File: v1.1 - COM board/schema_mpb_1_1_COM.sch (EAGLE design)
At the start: 4 parts, among them IC1 E73_2G4M04S, U1 ESP-WROOM-32

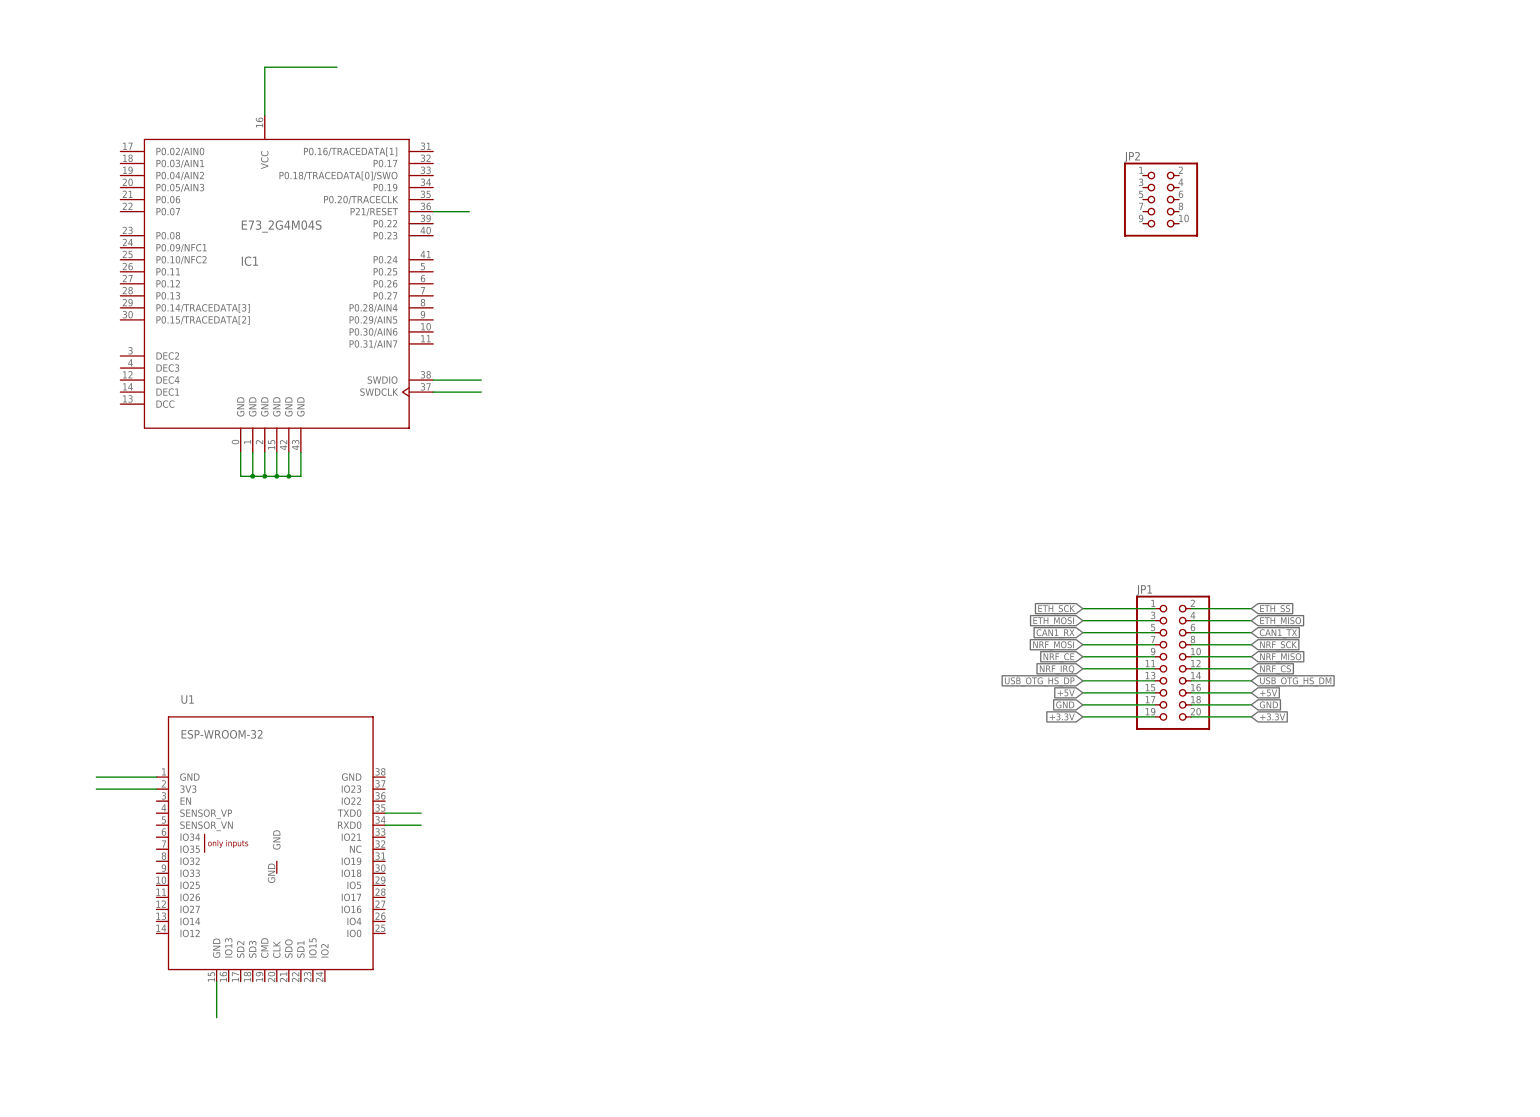
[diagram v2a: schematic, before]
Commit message: COM board
- Routed first version of Wireless COM board
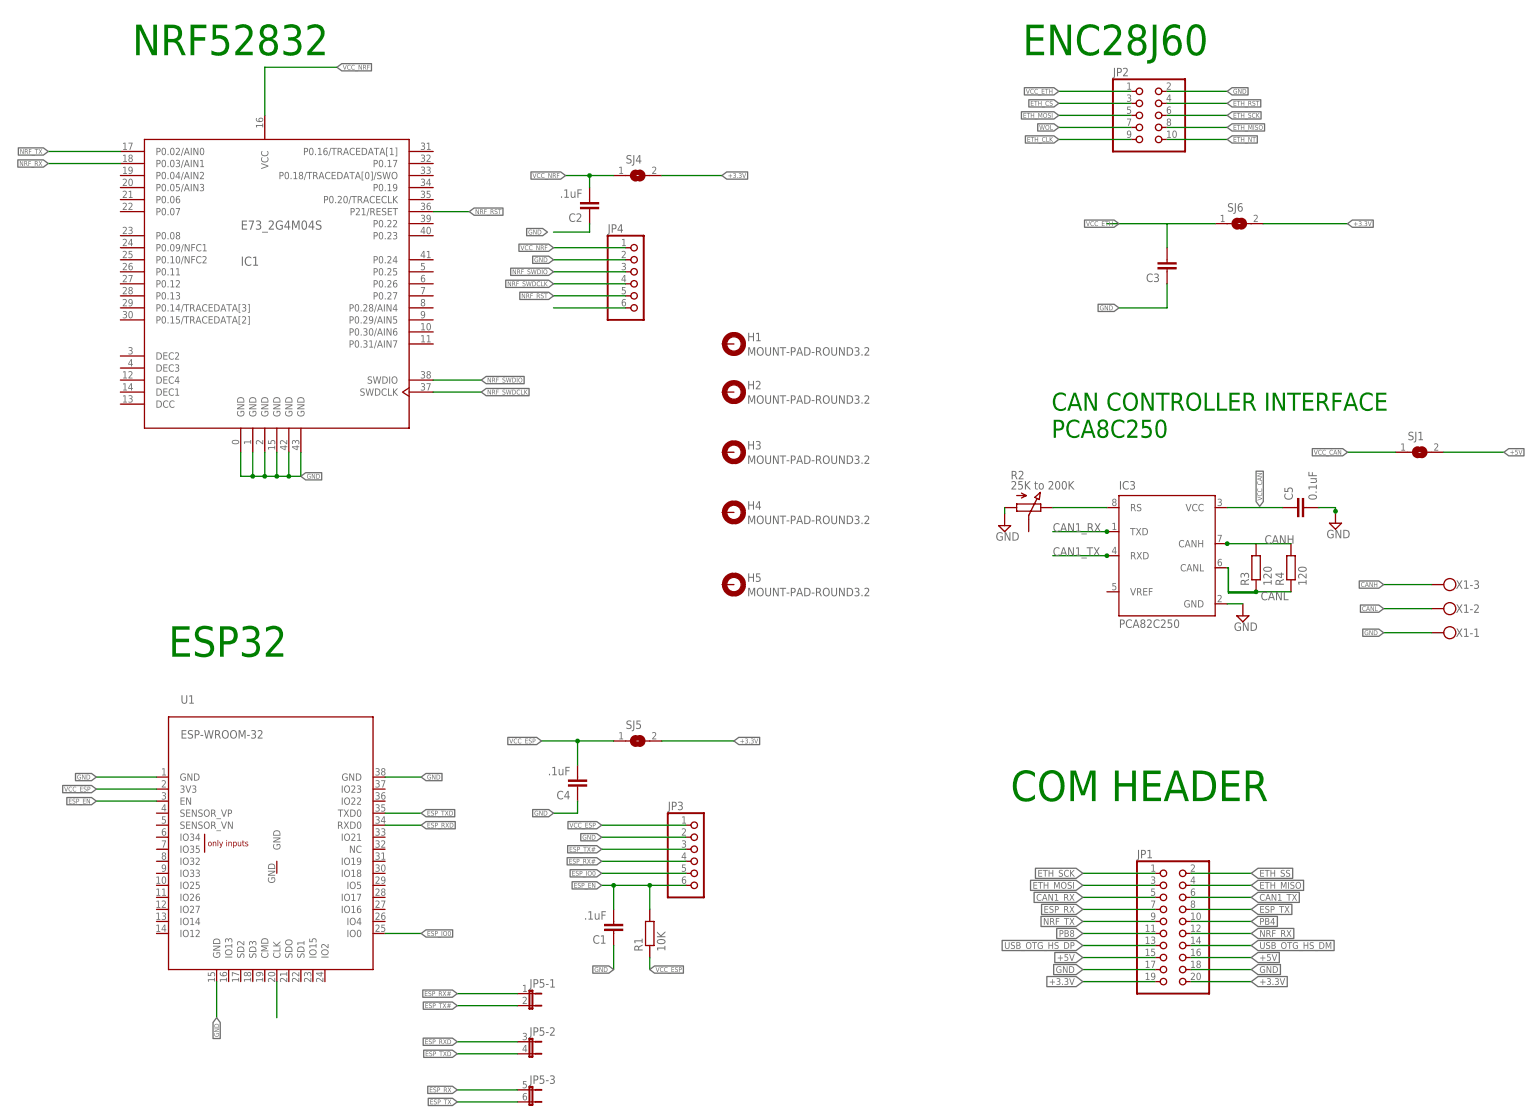
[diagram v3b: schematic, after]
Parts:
- added C1, C2, C4: .1uF, resistor:C-EUC0603
- added C3: (no value), resistor:C-EUC0603
- added C5: 0.1uF, resistor:C-EUC0805
- added H1, H2, H3, H4, H5: MOUNT-PAD-ROUND3.2, holes:MOUNT-PAD-ROUND3.2
- added IC3: PCA82C250, micro-philips:PCA82C250
- added JP3, JP4: (no value), pinhead:PINHD-1X6
- added JP5: (no value), jumper:JP3QE
- added R1: 10K, resistor:R-EU_R0603
- added R2: 25K to 200K, pot-vitrohm:PC25
- added R3, R4: 120, resistor:R-EU_R0805
- added SJ1, SJ4, SJ5, SJ6: (no value), jumper:SJW
- added X1: (no value), con-wago-500:W237-103
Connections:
- net NRF_IRQ renamed PB8
- net NRF_MISO renamed PB4
- removed net N$10: IC1.P21/RESET
- removed net N$2: U1.3V3
- removed net N$3: U1.TXD0
- removed net N$4: U1.RXD0
- removed net N$5: U1.GND@15
- removed net N$6: IC1.GND@1, IC1.GND@2, IC1.GND@3, IC1.GND@4, IC1.GND@5, IC1.GND@6
- removed net N$8: IC1.SWDCLK
- removed net N$9: IC1.VCC@1
- removed net NRF_CE: JP1.9
- removed net NRF_CS: JP1.12
- removed net NRF_MOSI: JP1.7
- removed net NRF_SCK: JP1.8
- new net CANH: IC3.CANH, R3.2, R4.2, X1-3.KL
- new net CANL: IC3.CANL, R3.1, R4.1, X1-2.KL
- new net ESP_EN: C1.2, JP3.6, R1.2, U1.EN
- new net ESP_IO0: JP3.5, U1.IO0
- new net ESP_RX: JP1.7, JP5-3.1
- new net ESP_RX#: JP3.4, JP5-1.1
- new net ESP_RXD: JP5-2.1, U1.RXD0
- new net ESP_TX: JP1.8, JP5-3.2
- new net ESP_TX#: JP3.3, JP5-1.2
- new net ESP_TXD: JP5-2.2, U1.TXD0
- new net ETH_CLK: JP2.9
- new net ETH_CS: JP2.3
- new net ETH_NT: JP2.10
- new net ETH_RST: JP2.4
- new net N$12: U1.CLK
- new net NRF_RST: IC1.P21/RESET, JP4.5
- new net NRF_RX: IC1.P0.03/AIN1, JP1.12
- new net NRF_SWDCLK: IC1.SWDCLK, JP4.4
- new net NRF_SWDIO: IC1.SWDIO, JP4.3
- new net NRF_TX: IC1.P0.02/AIN0, JP1.9
- new net VCC_CAN: C5.1, IC3.VCC, SJ1.1
- new net VCC_ESP: C4.2, JP3.1, R1.1, SJ5.1, U1.3V3
- new net VCC_ETH: C3.2, JP2.1, SJ6.1
- new net VCC_NRF: C2.2, IC1.VCC@1, JP4.1, SJ4.1
- new net WOL: JP2.7
- net +3.3V: now also SJ4.2, SJ5.2, SJ6.2
- net +5V: now also SJ1.2
- net CAN1_RX: now also IC3.TXD
- net CAN1_TX: now also IC3.RXD
- net ETH_MISO: now also JP2.8
- net ETH_MOSI: now also JP2.5
- net ETH_SCK: now also JP2.6
- net GND: now also C1.1, C2.1, C3.1, C4.1, C5.2, IC1.GND@1, IC1.GND@2, IC1.GND@3, IC1.GND@4, IC1.GND@5, IC1.GND@6, IC3.GND, JP2.2, JP3.2, JP4.2, R2.A, U1.GND@1, U1.GND@15, U1.GND@38, X1-1.KL
- net N$1: now also IC3.RS, R2.E; no longer U1.GND@1
- net N$7: now also JP4.6; no longer IC1.SWDIO
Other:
- note added: "CAN CONTROLLER INTERFACE PCA8C250"
- note added: "COM HEADER"
- note added: "ENC28J60"
- note added: "ESP32"
- note added: "NRF52832"
- moved on the sheet: JP1, JP2

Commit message: Logos
Added Geviton Logo to designs
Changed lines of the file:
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@@
 <layer number="56" name="wert" color="7" fill="1" visible="yes" active="no"/>
 <layer number="57" name="tCAD" color="7" fill="1" visible="yes" active="no"/>
+<layer number="59" name="tCarbon" color="7" fill="1" visible="no" active="no"/>
+<layer number="60" name="bCarbon" color="7" fill="1" visible="no" active="no"/>
 <layer number="88" name="SimResults" color="9" fill="1" visible="yes" active="yes"/>
 <layer number="89" name="SimProbes" color="9" fill="1" visible="yes" active="yes"/>
@@
 <layer number="127" name="_tValues" color="7" fill="1" visible="no" active="yes"/>
 <layer number="128" name="_bValues" color="7" fill="1" visible="no" active="yes"/>
+<layer number="129" name="Mask" color="7" fill="1" visible="yes" active="yes"/>
 <layer number="130" name="SMDSTROOK" color="7" fill="1" visible="yes" active="yes"/>
 <layer number="131" name="tAdjust" color="7" fill="1" visible="no" active="yes"/>
@@
 <layer number="223" name="223bmp" color="24" fill="1" visible="no" active="no"/>
 <layer number="224" name="224bmp" color="25" fill="1" visible="no" active="no"/>
+<layer number="225" name="225bmp" color="7" fill="1" visible="yes" active="yes"/>
+<layer number="226" name="226bmp" color="7" fill="1" visible="yes" active="yes"/>
+<layer number="227" name="227bmp" color="7" fill="1" visible="yes" active="yes"/>
+<layer number="228" name="228bmp" color="7" fill="1" visible="yes" active="yes"/>
+<layer number="229" name="229bmp" color="7" fill="1" visible="yes" active="yes"/>
+<layer number="230" name="230bmp" color="7" fill="1" visible="yes" active="yes"/>
 <layer number="231" name="Eagle3D_PG1" color="7" fill="1" visible="no" active="no"/>
 <layer number="232" name="Eagle3D_PG2" color="7" fill="1" visible="no" active="no"/>
@@
 </nets>
 </sheet>
+<sheet>
+<plain>
+</plain>
+<instances>
+</instances>
+<busses>
+</busses>
+<nets>
+</nets>
+</sheet>

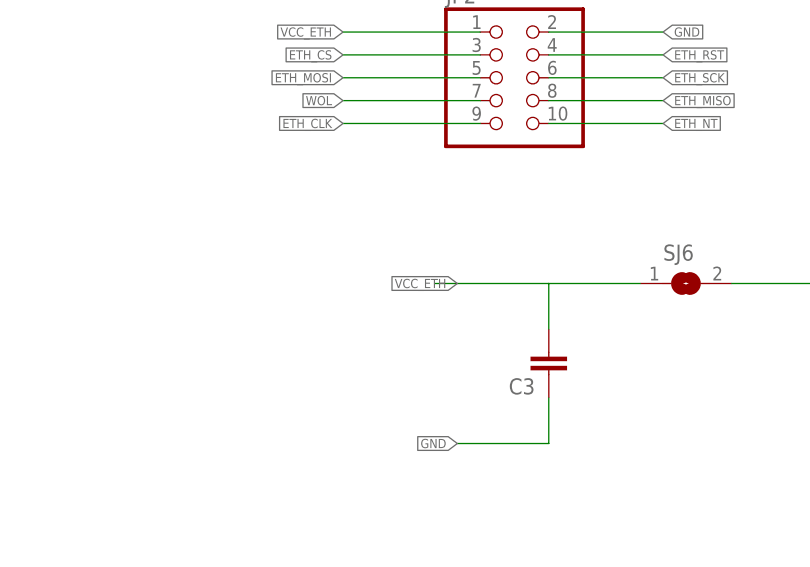
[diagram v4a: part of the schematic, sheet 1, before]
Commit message: Wireless board
- Changed drill sizes, got rid of via clearance issues
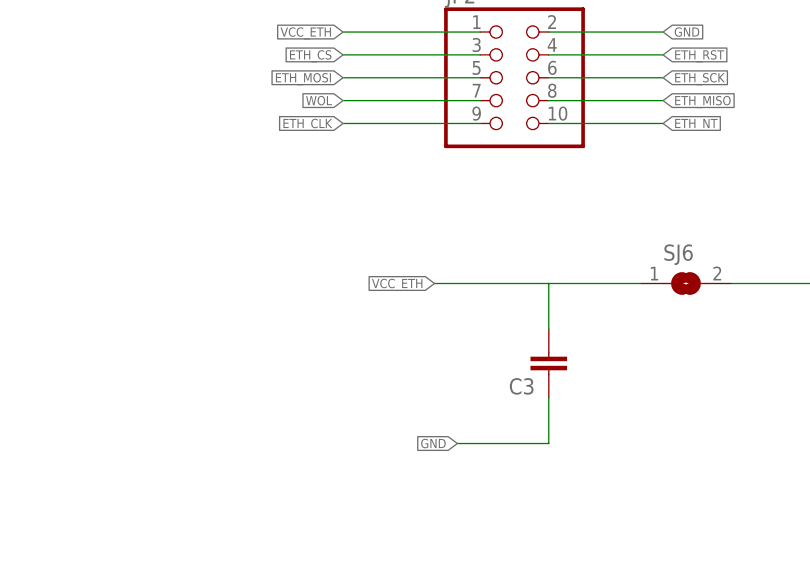
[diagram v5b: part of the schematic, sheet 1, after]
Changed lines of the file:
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@@
 <pinref part="SJ6" gate="1" pin="1"/>
 <wire x1="284.48" y1="200.66" x2="274.32" y2="200.66" width="0.1524" layer="91"/>
-<label x="264.16" y="200.66" size="1.016" layer="95" rot="R180" xref="yes"/>
+<label x="261.62" y="200.66" size="1.016" layer="95" rot="R180" xref="yes"/>
 <pinref part="C3" gate="G$1" pin="2"/>
 <wire x1="274.32" y1="200.66" x2="261.62" y2="200.66" width="0.1524" layer="91"/>
